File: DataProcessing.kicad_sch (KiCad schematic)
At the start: 0 parts

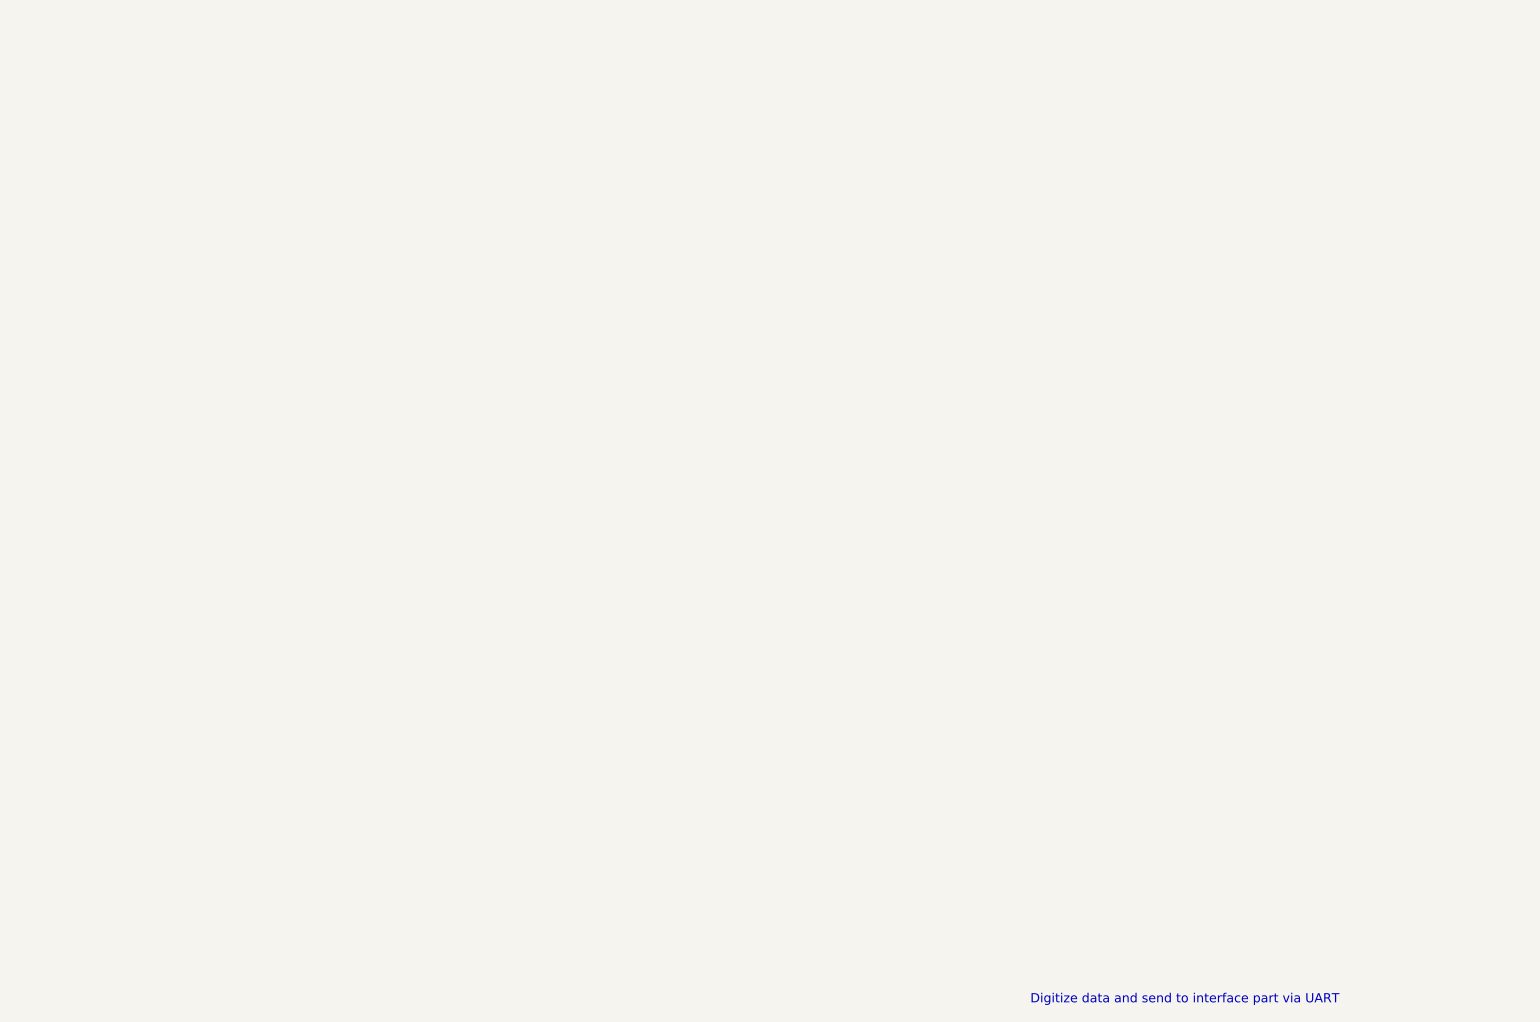
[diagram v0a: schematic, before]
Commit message: started dataprocessing
using a Atmega328PB
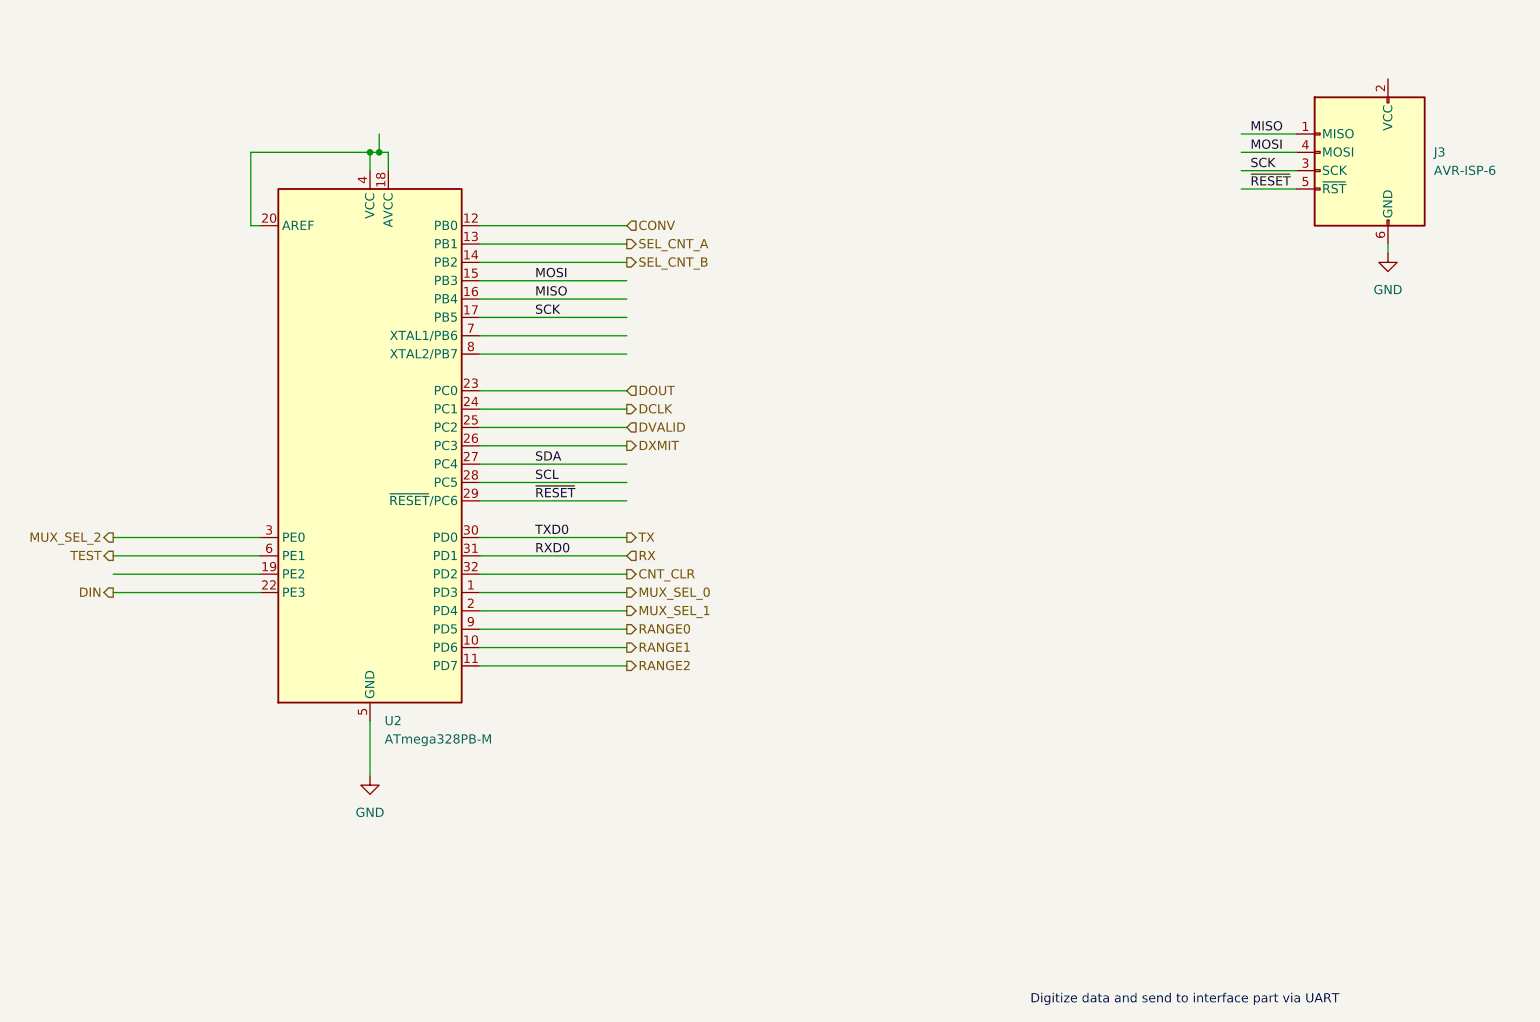
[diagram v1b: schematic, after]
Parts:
- added J3: AVR-ISP-6, Connector_PinHeader_2.54mm:PinHeader_2x03_P2.54mm_Vertical_SMD, symbol Connector:AVR-ISP-6
- added U2: ATmega328PB-M, Package_DFN_QFN:QFN-32-1EP_5x5mm_P0.5mm_EP3.1x3.1mm, symbol MCU_Microchip_ATmega:ATmega328PB-M
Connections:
- new net: U2.18 (AVCC), U2.20 (AREF), U2.4 (VCC)
- new net CNT_CLR: U2.32 (PD2)
- new net CONV: U2.12 (PB0)
- new net DCLK: U2.24 (PC1)
- new net DIN: U2.22 (PE3)
- new net DOUT: U2.23 (PC0)
- new net DVALID: U2.25 (PC2)
- new net DXMIT: U2.26 (PC3)
- new net GND: J3.6 (GND), U2.21 (GND), U2.33 (GND), U2.5 (GND)
- new net MISO: J3.1 (MISO), U2.16 (PB4)
- new net MOSI: J3.4 (MOSI), U2.15 (PB3)
- new net MUX_SEL_0: U2.1 (PD3)
- new net MUX_SEL_1: U2.2 (PD4)
- new net MUX_SEL_2: U2.3 (PE0)
- new net RANGE0: U2.9 (PD5)
- new net RANGE1: U2.10 (PD6)
- new net RANGE2: U2.11 (PD7)
- new net RX: U2.31 (PD1)
- new net SCK: J3.3 (SCK), U2.17 (PB5)
- new net SCL: U2.28 (PC5)
- new net SDA: U2.27 (PC4)
- new net SEL_CNT_A: U2.13 (PB1)
- new net SEL_CNT_B: U2.14 (PB2)
- new net TEST: U2.6 (PE1)
- new net TX: U2.30 (PD0)
- new net ~{RESET}: J3.5 (~{RST}), U2.29 (~{RESET}/PC6)

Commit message: connected the ICs to 5V digital power
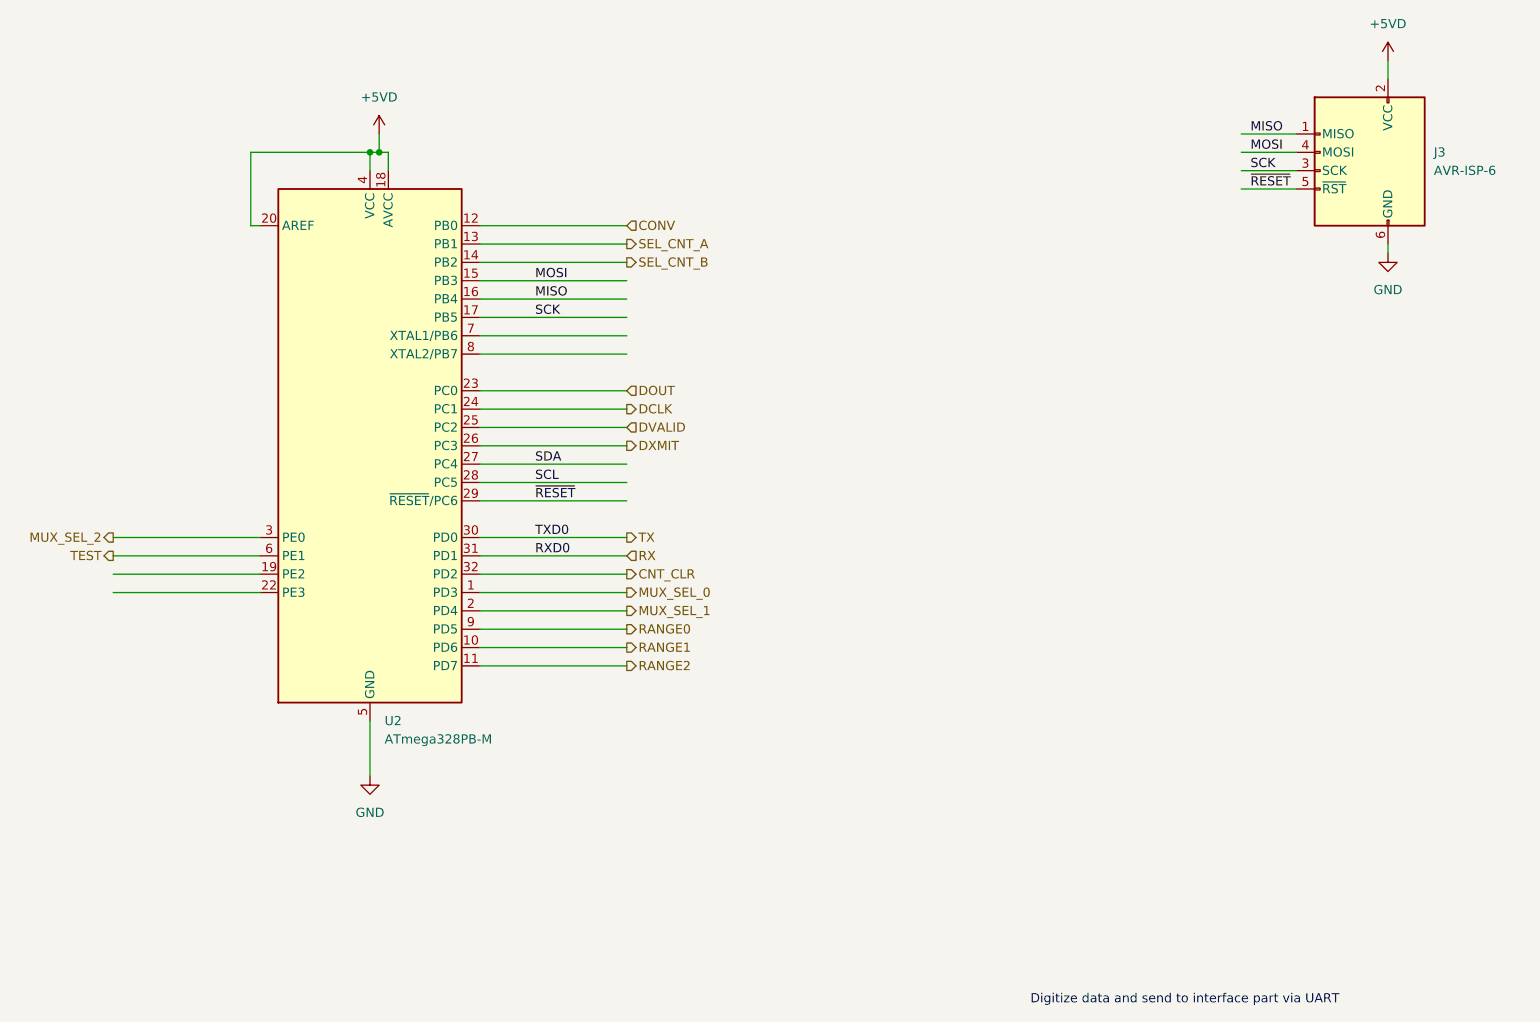
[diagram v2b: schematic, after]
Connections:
- net +5VD: now reaches J3.2 (VCC)
- net +5VD: now also U2.18 (AVCC), U2.20 (AREF), U2.4 (VCC)
- net DIN: no longer names the net of U2.22 (PE3)
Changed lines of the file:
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@@
+    (stroke (width 0) (type default) (color 0 0 0 0))
+  )
+  (wire (pts (xy 232.41 40.64) (xy 232.41 43.18))
     (stroke (width 0) (type default) (color 0 0 0 0))
   )
@@
     (effects (font (size 1.27 1.27)) (justify left))
   )
-  (hierarchical_label "DIN" (shape output) (at 55.88 114.3 180)
-    (effects (font (size 1.27 1.27)) (justify right))
-  )
   (hierarchical_label "CNT_CLR" (shape output) (at 127 111.76 0)
     (effects (font (size 1.27 1.27)) (justify left))
+  )
+  (symbol (lib_id "power:+5VD") (at 232.41 40.64 0) (unit 1)
+    (in_bom yes) (on_board yes) (fields_autoplaced)
+    (property "Reference" "#PWR?" (id 0) (at 232.41 44.45 0)
+      (effects (font (size 1.27 1.27)) hide)
+    )
+    (property "Value" "+5VD" (id 1) (at 232.41 35.56 0))
+    (property "Footprint" "" (id 2) (at 232.41 40.64 0)
+      (effects (font (size 1.27 1.27)) hide)
+    )
+    (property "Datasheet" "" (id 3) (at 232.41 40.64 0)
+      (effects (font (size 1.27 1.27)) hide)
+    )
+    (pin "1")
   )
   (symbol (lib_id "power:GND") (at 91.44 139.7 0) (unit 1)
@@
     (pin "9")
   )
+  (symbol (lib_id "power:+5VD") (at 92.71 50.8 0) (unit 1)
+    (in_bom yes) (on_board yes) (fields_autoplaced)
+    (property "Reference" "#PWR?" (id 0) (at 92.71 54.61 0)
+      (effects (font (size 1.27 1.27)) hide)
+    )
+    (property "Value" "+5VD" (id 1) (at 92.71 45.72 0))
+    (property "Footprint" "" (id 2) (at 92.71 50.8 0)
+      (effects (font (size 1.27 1.27)) hide)
+    )
+    (property "Datasheet" "" (id 3) (at 92.71 50.8 0)
+      (effects (font (size 1.27 1.27)) hide)
+    )
+    (pin "1")
+  )
   (symbol (lib_id "power:GND") (at 232.41 67.31 0) (unit 1)
